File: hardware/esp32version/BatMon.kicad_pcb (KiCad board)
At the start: 4 copper layers, 24 x 35 mm, 38 parts, among them J1 Battery_Connector, J3 Prog_Connector, J5 Charging_Connector, Q1 Q_PMOS_DDGSDD_TSOP-6, Q2 Q_PMOS_DDGSDD_TSOP-6, Q3 SS8050-G, Q4 SS8050-G, Q5 SS8050-G, SW1 POWER_SW, U1 ESP32-WROOM-32D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

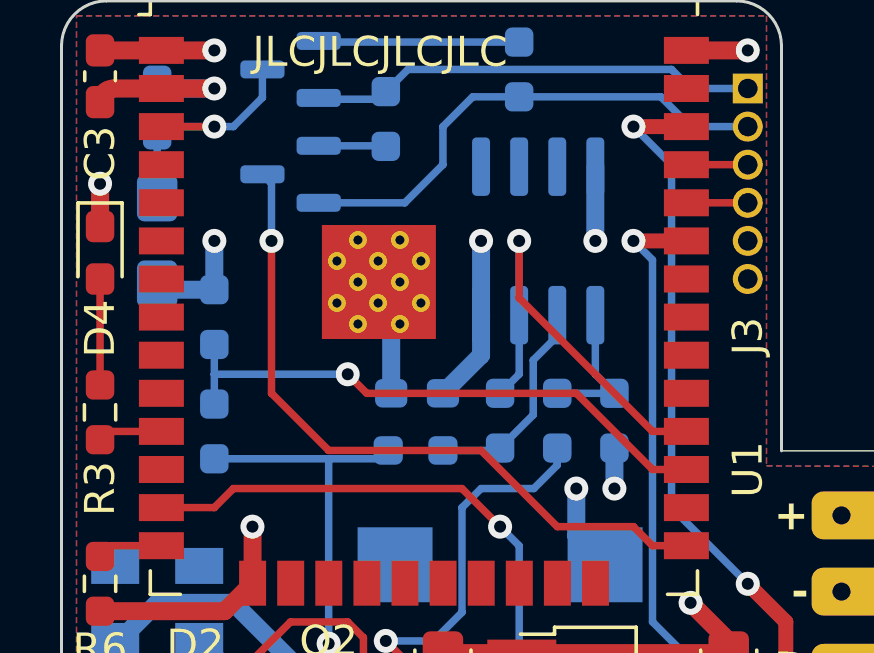
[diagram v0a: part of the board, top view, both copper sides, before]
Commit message: fixed battery inputs being connected to non ADC pins on uC (new board revision)
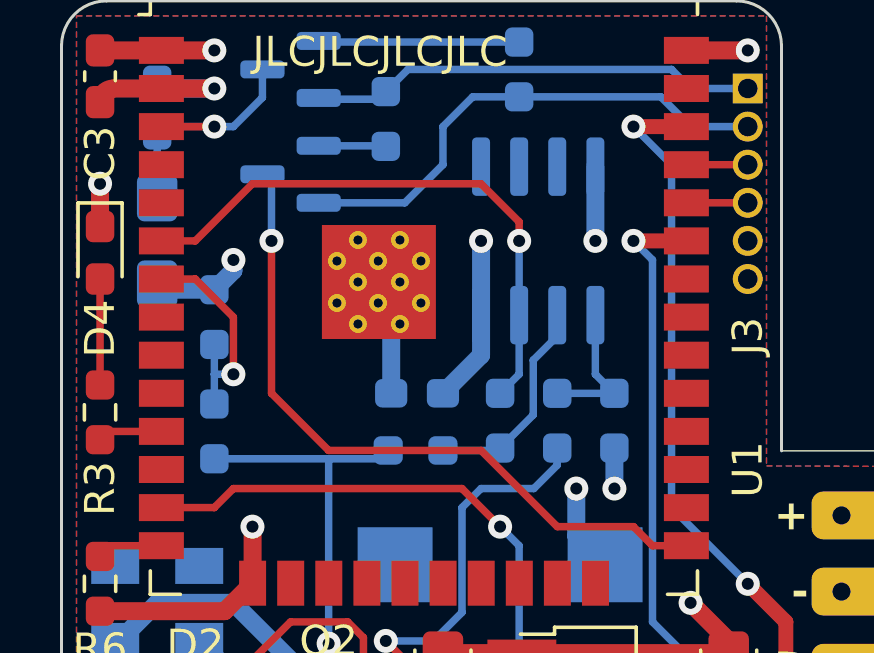
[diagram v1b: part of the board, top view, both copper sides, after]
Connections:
- U1 pad 27: C1ADC -> unconnected-(U1-IO16-Pad27)
- U1 pad 28: C2ADC -> unconnected-(U1-IO17-Pad28)
- U1 pad 6: unconnected-(U1-IO34-Pad6) -> C2ADC
- U1 pad 7: unconnected-(U1-IO35-Pad7) -> C1ADC
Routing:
- net C1ADC: track 19.0 -> 7.45 mm
- net C2ADC: track 14.7 -> 19.2 mm
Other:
- board text added: "BatMon ©fb 2023 23009 r2"
- board text removed: "BatMon ©fb 2023 23009"
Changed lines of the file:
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@@
   (net 14 "unconnected-(U1-SENSOR_VP-Pad4)")
   (net 15 "unconnected-(U1-SENSOR_VN-Pad5)")
-  (net 16 "unconnected-(U1-IO34-Pad6)")
-  (net 17 "unconnected-(U1-IO35-Pad7)")
+  (net 16 "unconnected-(U1-IO16-Pad27)")
+  (net 17 "unconnected-(U1-IO17-Pad28)")
   (net 18 "unconnected-(U1-IO32-Pad8)")
   (net 19 "unconnected-(U1-IO33-Pad9)")
@@
       (net 15 "unconnected-(U1-SENSOR_VN-Pad5)") (pinfunction "SENSOR_VN") (pintype "input+no_connect"))
     (pad "6" smd rect (at -8.75 -1.9) (size 1.5 0.9) (layers "F.Cu" "F.Paste" "F.Mask")
-      (net 16 "unconnected-(U1-IO34-Pad6)") (pinfunction "IO34") (pintype "input"))
+      (net 40 "C2ADC") (pinfunction "IO34") (pintype "input"))
     (pad "7" smd rect (at -8.75 -0.63) (size 1.5 0.9) (layers "F.Cu" "F.Paste" "F.Mask")
-      (net 17 "unconnected-(U1-IO35-Pad7)") (pinfunction "IO35") (pintype "input"))
+      (net 41 "C1ADC") (pinfunction "IO35") (pintype "input"))
     (pad "8" smd rect (at -8.75 0.64) (size 1.5 0.9) (layers "F.Cu" "F.Paste" "F.Mask")
       (net 18 "unconnected-(U1-IO32-Pad8)") (pinfunction "IO32") (pintype "bidirectional"))
@@
       (net 30 "unconnected-(U1-IO4-Pad26)") (pinfunction "IO4") (pintype "bidirectional+no_connect"))
     (pad "27" smd rect (at 8.75 5.72) (size 1.5 0.9) (layers "F.Cu" "F.Paste" "F.Mask")
-      (net 41 "C1ADC") (pinfunction "IO16") (pintype "bidirectional"))
+      (net 16 "unconnected-(U1-IO16-Pad27)") (pinfunction "IO16") (pintype "bidirectional"))
     (pad "28" smd rect (at 8.75 4.45) (size 1.5 0.9) (layers "F.Cu" "F.Paste" "F.Mask")
-      (net 40 "C2ADC") (pinfunction "IO17") (pintype "bidirectional"))
+      (net 17 "unconnected-(U1-IO17-Pad28)") (pinfunction "IO17") (pintype "bidirectional"))
     (pad "29" smd rect (at 8.75 3.18) (size 1.5 0.9) (layers "F.Cu" "F.Paste" "F.Mask")
       (net 31 "unconnected-(U1-IO5-Pad29)") (pinfunction "IO5") (pintype "bidirectional+no_connect"))
@@
     (effects (font (size 1 1) (thickness 0.25) bold) (justify left mirror))
   )
-  (gr_text "BatMon\n©fb 2023\n23009" (at 141.605 66.04 90) (layer "B.SilkS")
+  (gr_text "BatMon\n©fb 2023\n23009 r2" (at 141.605 66.04 90) (layer "B.SilkS")
     (effects (font (size 1 1) (thickness 0.15)) (justify left mirror))
   )
@@
   (segment (start 127.635 76.2) (end 129.54 76.2) (width 0.25) (layer "F.Cu") (net 38))
   (segment (start 130.065 76.725) (end 130.065 78.425) (width 0.25) (layer "F.Cu") (net 38))
-  (segment (start 135.255 63.5) (end 135.255 65.405) (width 0.25) (layer "F.Cu") (net 40))
-  (segment (start 139.7 69.85) (end 140.83 69.85) (width 0.25) (layer "F.Cu") (net 40))
-  (segment (start 135.255 65.405) (end 139.7 69.85) (width 0.25) (layer "F.Cu") (net 40))
+  (segment (start 123.33 63.5) (end 124.46 63.5) (width 0.25) (layer "F.Cu") (net 40))
+  (segment (start 126.365 61.595) (end 133.985 61.595) (width 0.25) (layer "F.Cu") (net 40))
+  (segment (start 133.985 61.595) (end 135.255 62.865) (width 0.25) (layer "F.Cu") (net 40))
+  (segment (start 124.46 63.5) (end 126.365 61.595) (width 0.25) (layer "F.Cu") (net 40))
+  (segment (start 135.255 62.865) (end 135.255 63.5) (width 0.25) (layer "F.Cu") (net 40))
   (via (at 135.255 63.5) (size 0.8) (drill 0.4) (layers "F.Cu" "B.Cu") (net 40))
   (segment (start 135.255 63.5) (end 135.255 67.945) (width 0.25) (layer "B.Cu") (net 40))
   (segment (start 135.255 67.945) (end 134.62 68.58) (width 0.25) (layer "B.Cu") (net 40))
-  (segment (start 139.7 71.12) (end 140.83 71.12) (width 0.25) (layer "F.Cu") (net 41))
-  (segment (start 130.175 68.58) (end 137.16 68.58) (width 0.25) (layer "F.Cu") (net 41))
-  (segment (start 129.54 67.945) (end 130.175 68.58) (width 0.25) (layer "F.Cu") (net 41))
-  (segment (start 137.16 68.58) (end 139.7 71.12) (width 0.25) (layer "F.Cu") (net 41))
-  (via (at 129.54 67.945) (size 0.8) (drill 0.4) (layers "F.Cu" "B.Cu") (net 41))
+  (segment (start 124.46 64.77) (end 123.33 64.77) (width 0.25) (layer "F.Cu") (net 41))
+  (segment (start 125.73 67.945) (end 125.73 66.04) (width 0.25) (layer "F.Cu") (net 41))
+  (segment (start 125.73 66.04) (end 124.46 64.77) (width 0.25) (layer "F.Cu") (net 41))
+  (via (at 125.73 67.945) (size 0.8) (drill 0.4) (layers "F.Cu" "B.Cu") (net 41))
   (segment (start 125.095 67.945) (end 125.095 66.9525) (width 0.25) (layer "B.Cu") (net 41))
+  (segment (start 125.095 67.945) (end 125.73 67.945) (width 0.25) (layer "B.Cu") (net 41))
   (segment (start 125.095 68.9375) (end 125.095 67.945) (width 0.25) (layer "B.Cu") (net 41))
-  (segment (start 125.095 67.945) (end 129.54 67.945) (width 0.25) (layer "B.Cu") (net 41))
   (segment (start 123.33 69.85) (end 121.5625 69.85) (width 0.25) (layer "F.Cu") (net 42))
   (segment (start 121.5625 69.85) (end 121.285 70.1275) (width 0.25) (layer "F.Cu") (net 42))
@@
   (via (at 125.095 57.15) (size 0.8) (drill 0.4) (layers "F.Cu" "B.Cu") (free) (net 44))
   (via (at 140.335 81.915) (size 0.8) (drill 0.4) (layers "F.Cu" "B.Cu") (net 44))
-  (via (at 125.095 63.5) (size 0.8) (drill 0.4) (layers "F.Cu" "B.Cu") (net 44))
+  (via (at 125.73 64.135) (size 0.8) (drill 0.4) (layers "F.Cu" "B.Cu") (net 44))
   (via (at 138.43 71.755) (size 0.8) (drill 0.4) (layers "F.Cu" "B.Cu") (net 44))
   (segment (start 141.7 82.08) (end 141.535 81.915) (width 0.6) (layer "B.Cu") (net 44))
   (segment (start 125.095 65.1275) (end 123.38 65.1275) (width 0.6) (layer "B.Cu") (net 44))
   (segment (start 140.335 83.185) (end 140.335 81.915) (width 0.6) (layer "B.Cu") (net 44))
+  (segment (start 125.73 64.4925) (end 125.095 65.1275) (width 0.6) (layer "B.Cu") (net 44))
   (segment (start 140.015 83.505) (end 140.335 83.185) (width 0.6) (layer "B.Cu") (net 44))
   (segment (start 137.795 61.025) (end 137.795 63.5) (width 0.6) (layer "B.Cu") (net 44))
   (segment (start 141.7 80.3) (end 142.3625 79.6375) (width 0.6) (layer "B.Cu") (net 44))
   (segment (start 142.3625 79.6375) (end 142.3625 79) (width 0.6) (layer "B.Cu") (net 44))
+  (segment (start 125.73 64.135) (end 125.73 64.4925) (width 0.6) (layer "B.Cu") (net 44))
   (segment (start 130.99 68.58) (end 130.99 66.56) (width 0.6) (layer "B.Cu") (net 44))
   (segment (start 141.535 81.915) (end 140.335 81.915) (width 0.6) (layer "B.Cu") (net 44))
@@
   (segment (start 123.38 65.1275) (end 123.19 64.9375) (width 0.6) (layer "B.Cu") (net 44))
   (segment (start 141.7 82.88) (end 141.7 80.48) (width 0.6) (layer "B.Cu") (net 44))
-  (segment (start 125.095 65.1275) (end 125.095 63.5) (width 0.6) (layer "B.Cu") (net 44))
   (segment (start 130.99 66.56) (end 131.28 66.27) (width 0.6) (layer "B.Cu") (net 44))
   (segment (start 140.015 84.7875) (end 140.015 83.505) (width 0.6) (layer "B.Cu") (net 44))
